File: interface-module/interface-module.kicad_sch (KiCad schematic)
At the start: 10 parts, among them J1 Conn_01x08, J2 Conn_01x08, J3 Conn_01x02, SW1 SW_Coded_SH-7050

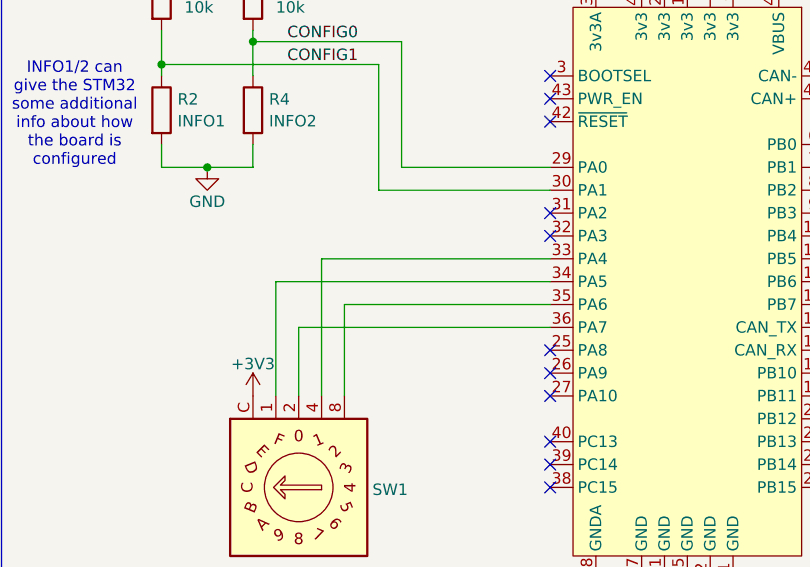
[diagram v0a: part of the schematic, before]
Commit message: Added address pin labels
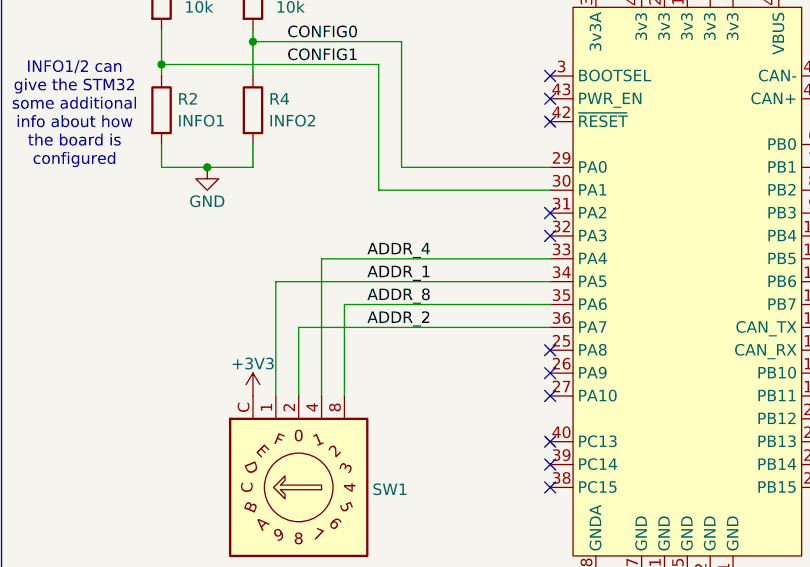
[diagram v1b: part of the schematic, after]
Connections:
- net ADDR_1: now reaches SW1.1, U1.34 (PA5)
- net ADDR_2: now reaches SW1.2, U1.36 (PA7)
- net ADDR_4: now reaches SW1.4, U1.33 (PA4)
- net ADDR_8: now reaches SW1.8, U1.35 (PA6)
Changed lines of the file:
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@@
+		)
+	)
+	(label "ADDR_2"
+		(at 59.69 78.74 0)
+		(fields_autoplaced yes)
+		(effects
+			(font
+				(size 1.27 1.27)
+			)
+			(justify left bottom)
+		)
+	)
+	(label "ADDR_4"
+		(at 59.69 71.12 0)
+		(fields_autoplaced yes)
+		(effects
+			(font
+				(size 1.27 1.27)
+			)
+			(justify left bottom)
+		)
+	)
+	(label "ADDR_1"
+		(at 59.69 73.66 0)
+		(fields_autoplaced yes)
+		(effects
+			(font
+				(size 1.27 1.27)
+			)
+			(justify left bottom)
+		)
+	)
+	(label "ADDR_8"
+		(at 59.69 76.2 0)
+		(fields_autoplaced yes)
+		(effects
+			(font
+				(size 1.27 1.27)
+			)
+			(justify left bottom)
 		)
 	)

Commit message: Upgraded to v1.1.
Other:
- company: (none) -> Portland State Aerosapce Society
- title: (none) -> MinTS Interface Module
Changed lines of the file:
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@@
 	(generator_version "9.0")
 	(paper "USLedger")
+	(title_block
+		(title "MinTS Interface Module")
+		(date "2025-12-23")
+		(rev "1.1")
+		(company "Portland State Aerosapce Society")
+	)
 	(rectangle
 		(start 19.05 118.11)

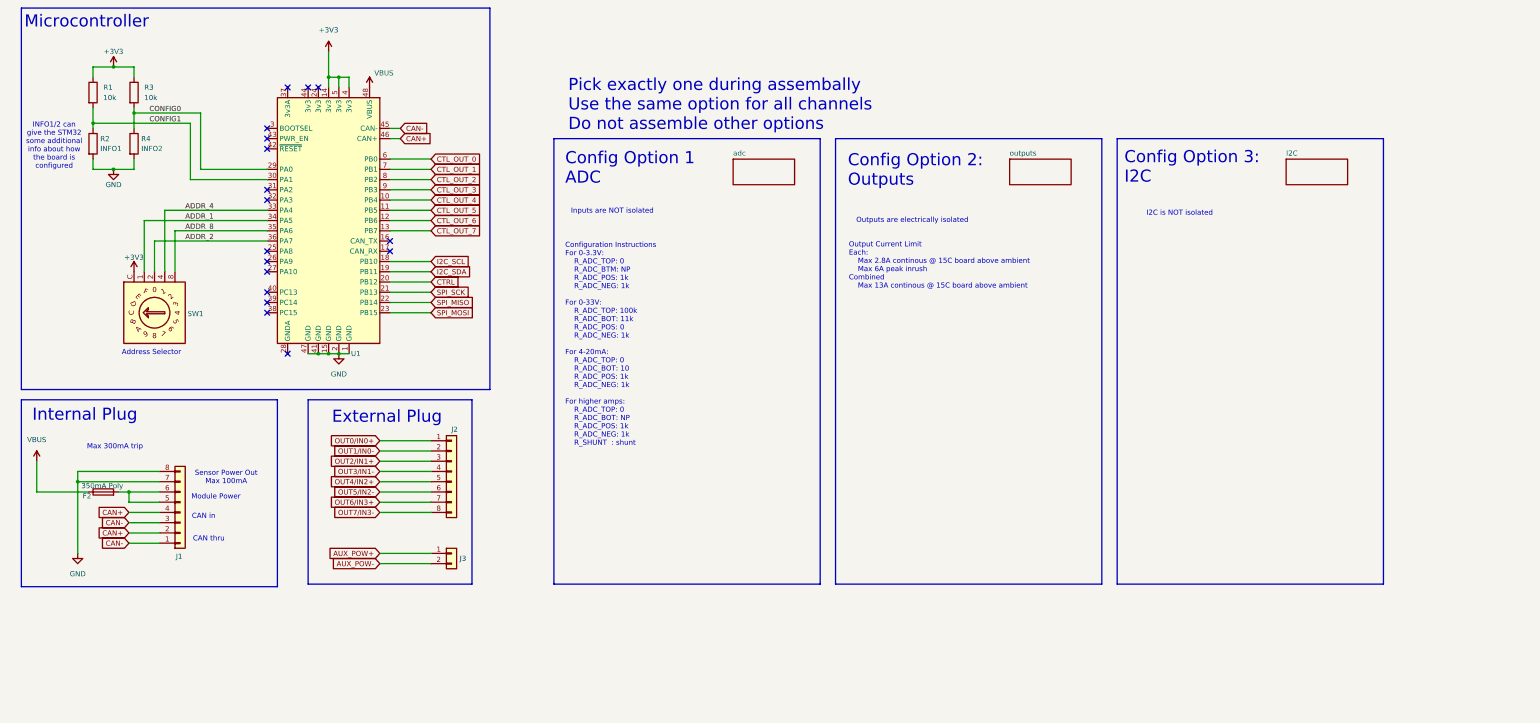
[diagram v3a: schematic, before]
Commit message: Final polish before manufacturing (v1.1)
Upped version to 1.1. Cleared ERC errors, one interesting one left that won't stop manufacturing. Cleared all DRC warnings and
errors. Formatted BOM. Fixed BOM for important parts. Added fuse parts for reference. Cleaned up silkscreen.
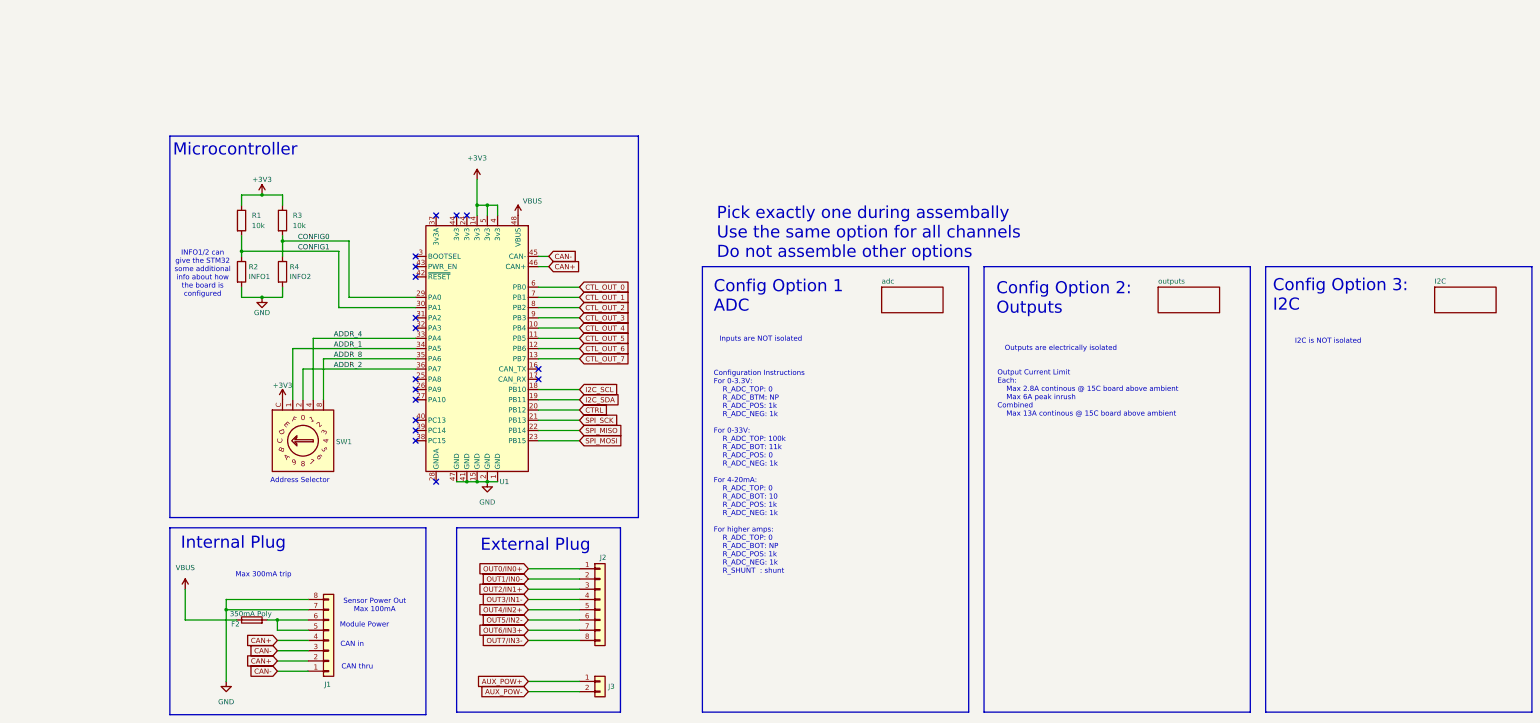
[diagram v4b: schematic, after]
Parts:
- F2: DIS (none) -> DigiKey; MFR (none) -> Littelfuse
- J1, J2: DIS (none) -> DigiKey; MFR (none) -> Same Sky
- J3: footprint TerminalBlock:TerminalBlock_bornier-2_P5.08mm -> TerminalBlock_Phoenix:TerminalBlock_Phoenix_MKDS-1,5-2-5.08_1x02_P5.08mm_Horizontal; DIS (none) -> DigiKey; MFR (none) -> Phoenix
- R1, R2, R3, R4: DIS (none) -> DigiKey
- SW1: DIS (none) -> DigiKey; MFR (none) -> CTS
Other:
- moved on the sheet: F2, J1, J2, J3, R1, R2, R3, R4, SW1, U1

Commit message: Fix MCP reference name to specify MCP3464R model and move to KiCad 10
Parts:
- U1: value ~ -> (none)
